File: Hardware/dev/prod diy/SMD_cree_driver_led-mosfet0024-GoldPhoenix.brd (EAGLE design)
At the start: 19.7 x 34 mm, 15 parts, among them Q1 BSS123, Q2 BSS123, Q3 BSS123, Q4 BSS123, Q5 NSI50350AST3G, Q6 NSI50350AST3G, Q7 NSI50350AST3G, Q8 NSI50350AST3G

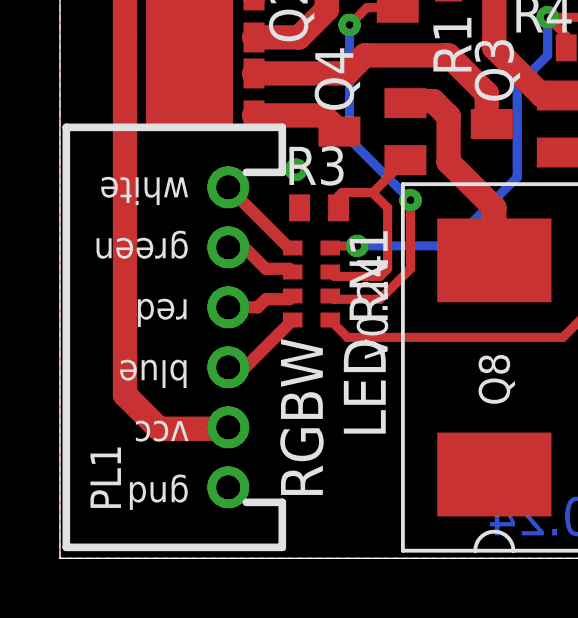
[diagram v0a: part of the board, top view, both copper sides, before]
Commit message: fixed silk error on LED board
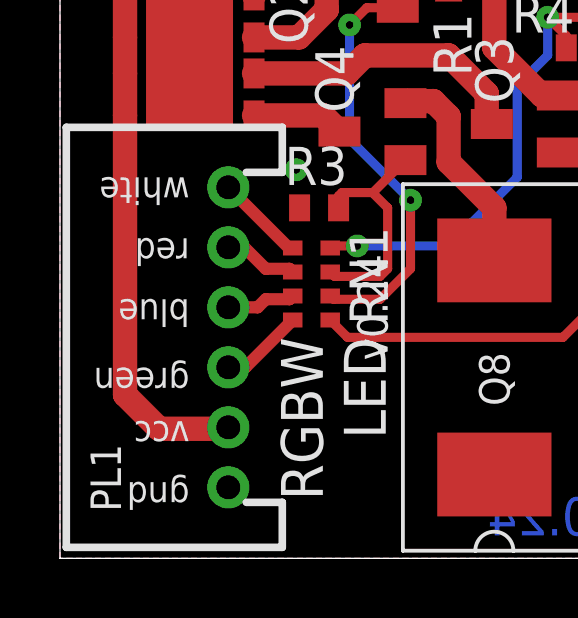
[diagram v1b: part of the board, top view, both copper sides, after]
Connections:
- net BLUE renamed _RED
- net BLUE_OUT renamed GREEN_PWM_IN
- net GREEN renamed _BLUE
- net GREEN_OUT renamed RED_PWM_IN
- net N$1 renamed BLUE_DRIVER
- net N$13 renamed WHITE_DRIVER
- net N$2 renamed GREEN_DRIVER
- net N$3 renamed RED_DRIVER
- net N$5 renamed WHITE_PWM_IN
- net RED renamed _GREEN
- net RED_OUT renamed BLUE_PWM_IN
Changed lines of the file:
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@@
 <text x="30.734" y="19.812" size="1.27" layer="16" font="vector" ratio="20" rot="MR0">V 0.24</text>
 <text x="15.748" y="31.75" size="0.889" layer="21" font="vector" rot="SR180">white</text>
-<text x="15.748" y="29.718" size="0.889" layer="21" font="vector" rot="SR180">green</text>
-<text x="15.748" y="27.686" size="0.889" layer="21" font="vector" rot="SR180">red</text>
-<text x="15.748" y="25.654" size="0.889" layer="21" font="vector" rot="SR180">blue</text>
+<text x="15.748" y="25.4" size="0.889" layer="21" font="vector" rot="SR180">green</text>
+<text x="15.748" y="29.718" size="0.889" layer="21" font="vector" rot="SR180">red</text>
+<text x="15.748" y="27.686" size="0.889" layer="21" font="vector" rot="SR180">blue</text>
 <text x="15.748" y="23.622" size="0.889" layer="21" font="vector" rot="SR180">vcc</text>
 <text x="15.748" y="21.59" size="0.889" layer="21" font="vector" rot="SR180">gnd</text>
@@
 <via x="19.304" y="32.004" extent="1-16" drill="0.254"/>
 </signal>
-<signal name="BLUE" class="1">
+<signal name="_RED" class="1">
 <contactref element="Q4" pad="1"/>
 <contactref element="R3" pad="2"/>
@@
 <wire x1="21.862" y1="31.242" x2="21.844" y2="31.242" width="0.3048" layer="1"/>
 </signal>
-<signal name="RED" class="1">
+<signal name="_GREEN" class="1">
 <contactref element="Q3" pad="1"/>
 <contactref element="R2" pad="2"/>
@@
 <wire x1="29.672" y1="32.578" x2="28.024" y2="32.578" width="0.3048" layer="1"/>
 </signal>
-<signal name="GREEN" class="1">
+<signal name="_BLUE" class="1">
 <contactref element="Q2" pad="1"/>
 <contactref element="R1" pad="2"/>
@@
 <wire x1="23.01" y1="34.29" x2="22.944" y2="34.224" width="0.8128" layer="1"/>
 </signal>
-<signal name="N$3">
+<signal name="RED_DRIVER">
 <contactref element="Q4" pad="3"/>
 <contactref element="U$1" pad="8"/>
@@
 <wire x1="20.204" y1="33.814" x2="20.744" y2="33.274" width="0.8128" layer="1"/>
 </signal>
-<signal name="N$1">
+<signal name="BLUE_DRIVER">
 <contactref element="Q2" pad="3"/>
 <contactref element="U$1" pad="6"/>
@@
 <wire x1="20.32" y1="38.184" x2="20.49" y2="38.354" width="0.8128" layer="1"/>
 </signal>
-<signal name="N$2">
+<signal name="GREEN_DRIVER">
 <contactref element="Q3" pad="3"/>
 <contactref element="U$1" pad="7"/>
@@
 <wire x1="21.8694" y1="48.7934" x2="21.8694" y2="49.53" width="0.8128" layer="1"/>
 </signal>
-<signal name="GREEN_OUT" class="1">
+<signal name="RED_PWM_IN" class="1">
 <contactref element="PL1" pad="2"/>
 <contactref element="RN1" pad="2"/>
@@
 <wire x1="19.079" y1="28.702" x2="19.187" y2="28.594" width="0.4064" layer="1"/>
 </signal>
-<signal name="RED_OUT" class="1">
+<signal name="BLUE_PWM_IN" class="1">
 <contactref element="PL1" pad="3"/>
 <contactref element="RN1" pad="3"/>
@@
 <wire x1="19.079" y1="27.686" x2="19.187" y2="27.794" width="0.4064" layer="1"/>
 </signal>
-<signal name="BLUE_OUT" class="1">
+<signal name="GREEN_PWM_IN" class="1">
 <contactref element="PL1" pad="4"/>
 <contactref element="RN1" pad="4"/>
@@
 <contactref element="U$1" pad="P$1"/>
 </signal>
-<signal name="N$5">
+<signal name="WHITE_PWM_IN">
 <contactref element="PL1" pad="1"/>
 <contactref element="RN1" pad="1"/>
@@
 <wire x1="29.548" y1="41.0386" x2="27.686" y2="42.9006" width="0.8128" layer="1"/>
 </signal>
-<signal name="N$13">
+<signal name="WHITE_DRIVER">
 <contactref element="Q1" pad="3"/>
 <contactref element="U$1" pad="5"/>
